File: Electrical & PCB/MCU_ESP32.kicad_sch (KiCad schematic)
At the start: 31 parts, among them J100 TF-01A, J101 Conn_01x04_Male, J20 Screw_Terminal_01x03, J21 Conn_01x02_Male, Q2 SS8050-G, Q3 SS8050-G, Q5 PMPB23XNEZ, SW1 SW_Push, SW2 SW_Push, U1 ESP32-WROOM-32U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

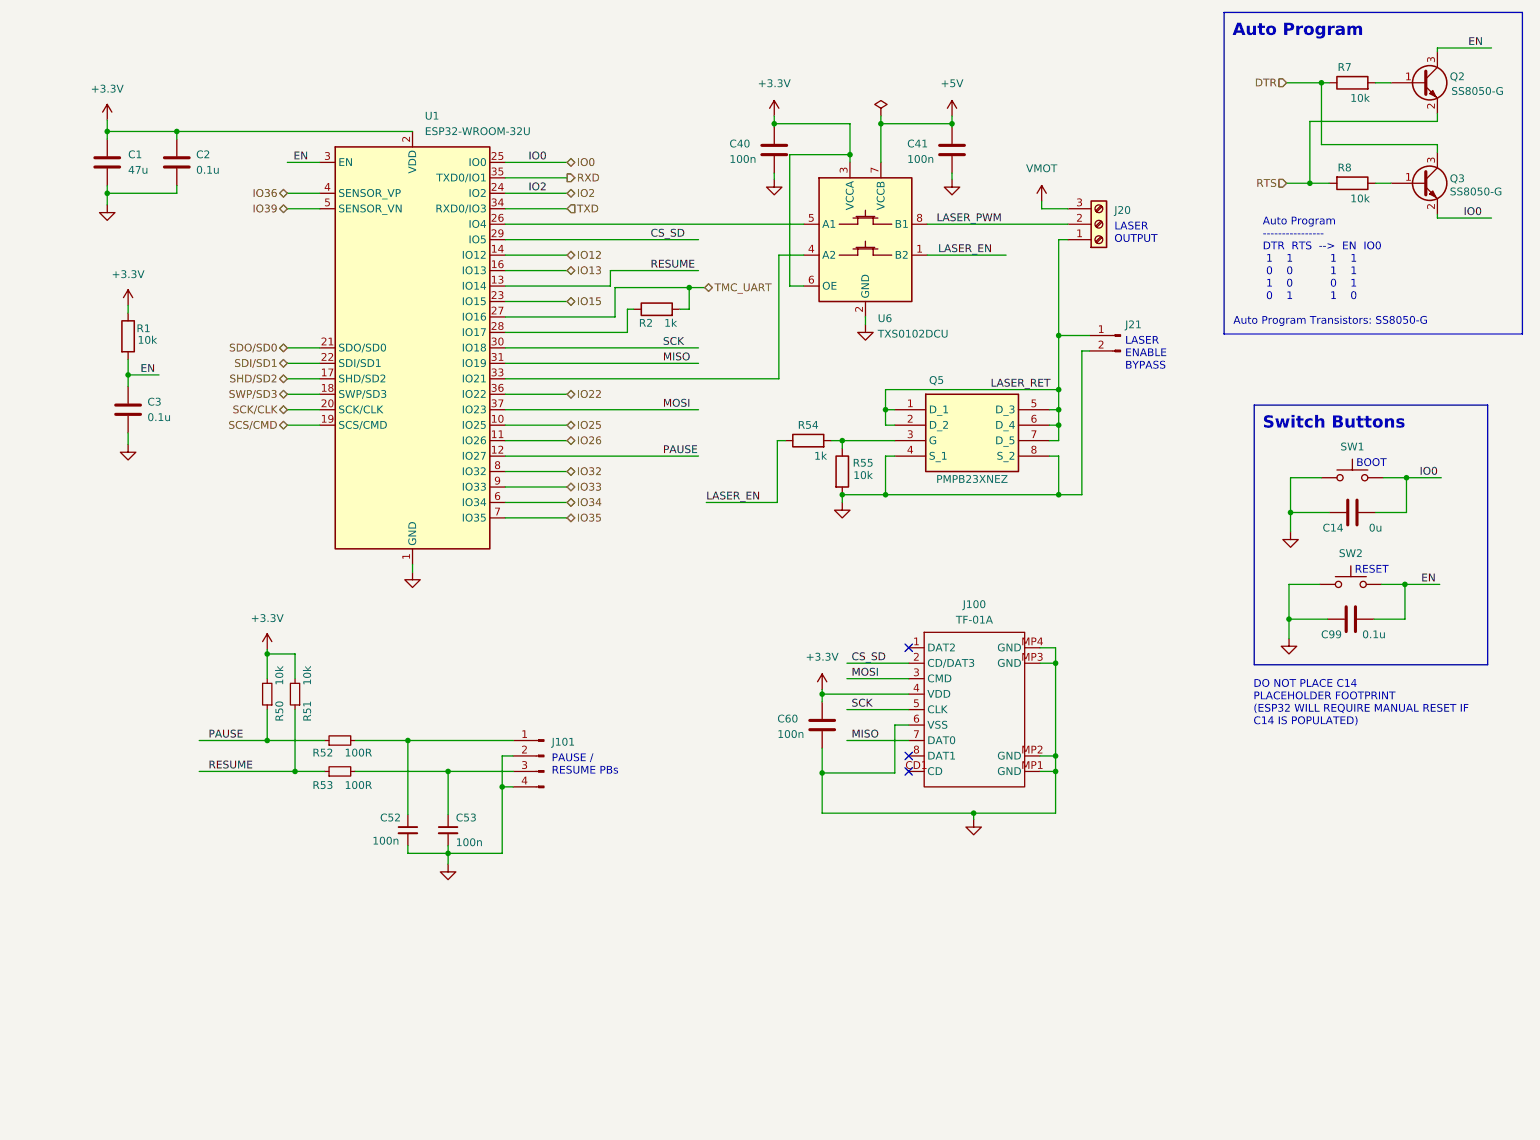
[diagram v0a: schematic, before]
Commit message: Electrical schematic & PCB layout udpate
Updated to allow selection / bypass of 3.3V - 5V level converter on laser PWM signal. Laser enable now 3V3 from MCU instead of level converting. This should prevent laser from actuating at power up due to level converter momentarily pulling outputs high at startup.
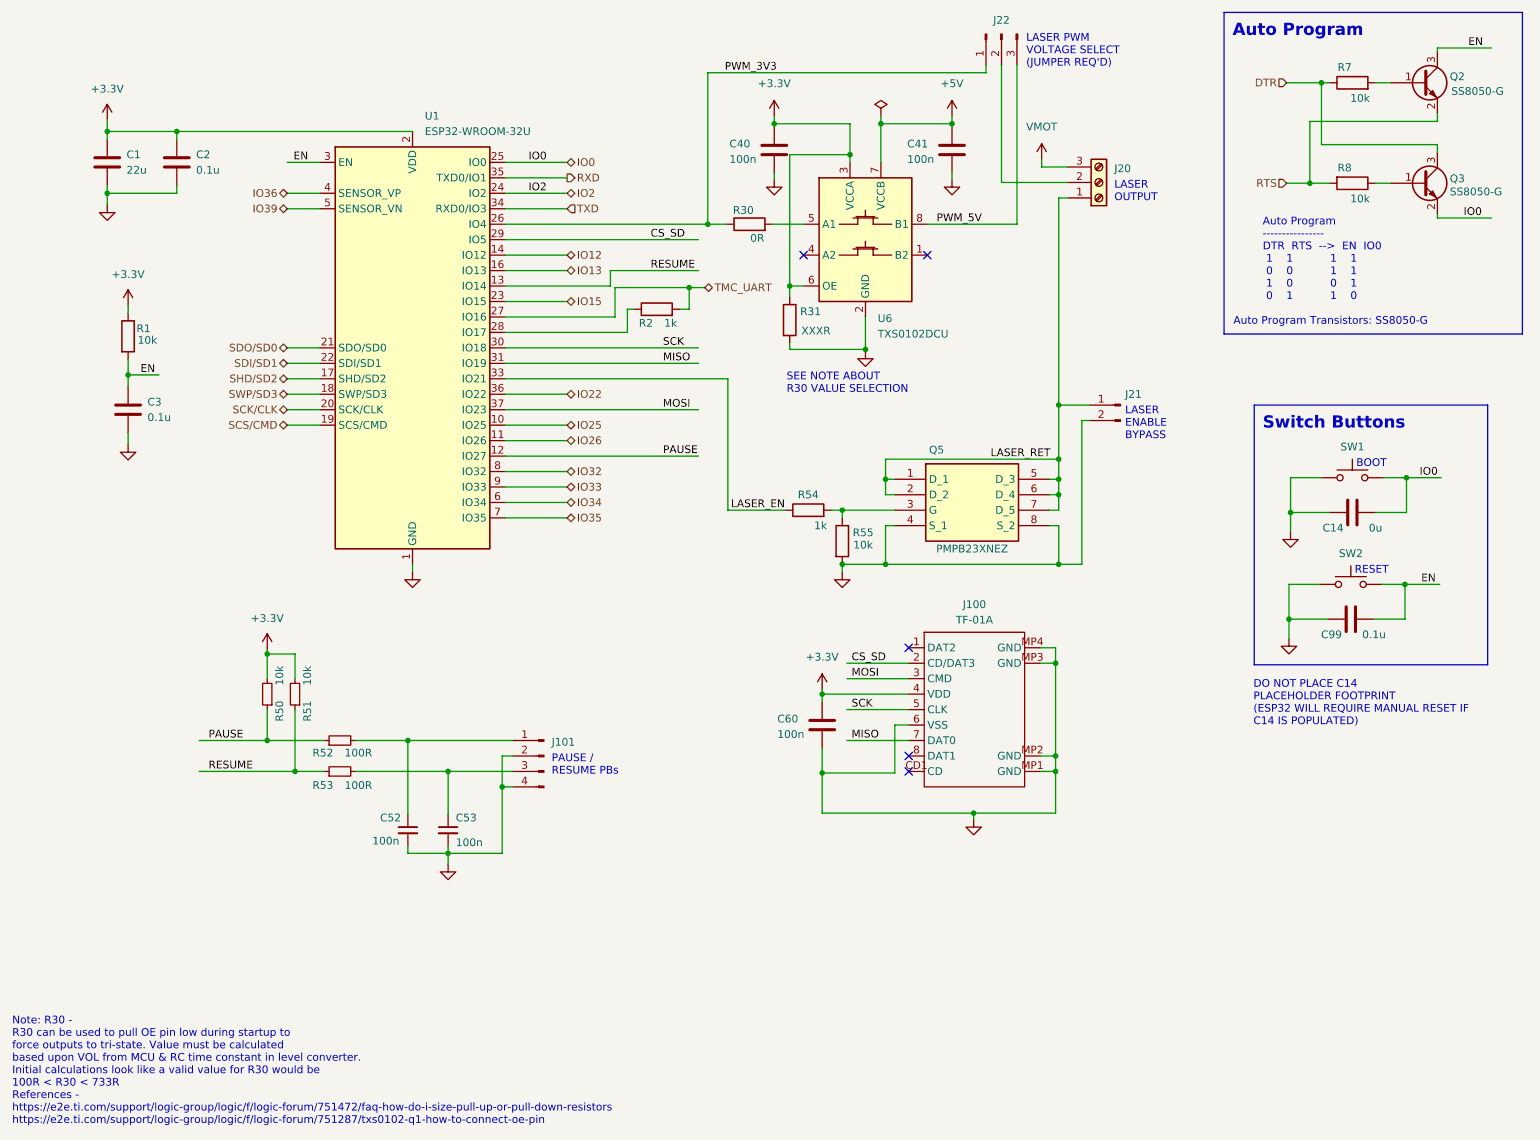
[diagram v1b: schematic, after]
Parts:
- added J22: Conn_01x03_Male, Connector_PinHeader_2.54mm:PinHeader_1x03_P2.54mm_Vertical, symbol Connector:Conn_01x03_Male
- added R30: 0R, Resistor_SMD:R_0603_1608Metric, symbol Device:R
- added R31: XXXR, Resistor_SMD:R_0603_1608Metric, symbol Device:R
- C1: value 47u -> 22u
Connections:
- net +3.3V: now also R31.1
- net GND: now also R31.2
- net LASER_EN: now also U1.33 (IO21); no longer U6.1 (B2)
- net at U6.5 (A1): now also R30.2; no longer U1.26 (IO4)
- net at U6.4 (A2): no longer U1.33 (IO21)
- net LASER_PWM: no longer names the net of J20.2 (Pin_2)
- net LASER_PWM: now also J22.2 (Pin_2); no longer U6.8 (B1)
- new net PWM_3V3: J22.1 (Pin_1), R30.1, U1.26 (IO4)
- new net PWM_5V: J22.3 (Pin_3), U6.8 (B1)
- no-connect marks 3 -> 5
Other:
- note added: "LASER PWM VOLTAGE SELECT (JUMPER REQ'D)"
- note added: "Note: R30 - R30 can be used to pull OE pin low during startup to force outputs to tri-state. Value must be calculated based upon VOL from MCU & RC time constant in level converter. Initial calculations look like a valid value for R30 would be 100R < R30 < 733R References - https://e2e.ti.com/support/logic-group/logic/f/logic-forum/751472/faq-how-do-i-size-pull-up-or-pull-down-resistors https://e2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"
- note added: "SEE NOTE ABOUT R30 VALUE SELECTION"
- moved on the sheet: J20, J21, Q5, R54, R55
